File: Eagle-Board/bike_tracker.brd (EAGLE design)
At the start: 70 x 33 mm, 93 parts, among them IC1 24C00TS, IC2 BME280/680, J1 TRANSFLASH-LOCK, Q1 IRLML5203, Q2 IRLML5203, Q3 IRLML5203, Q4 IRLML5203, U1 MPU-9250/5

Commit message: minor modifications
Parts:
- moved D1 0.15 mm to (43.4, 61.9)

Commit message: last minute modifications added
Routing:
- net VBAT+: track 28.9 -> 25.1 mm

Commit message: wireless charging option added
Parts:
- added C29, C30: 22nF, resistor:C0603
- added C31, C32: 0.47uF, resistor:C0603
- added C33, C34: 0.01uF, resistor:C0603
- added C35: 100pF, resistor:C0603
- added C36: 1800pF, resistor:C0603
- added C37: 47nF, resistor:C0603
- added C38, C39: 68nF, resistor:C0603
- added C40, C41: 10uF, sparkfun:1206
- added C42, C44, C45: 0.1uF, resistor:C0603
- added C43: 1.0uF, resistor:C0603
- added COIL: 332-02, con-garry:332-02
- added D2: MBR0520, microduino:SOD123
- added R48: 196, resistor:R0603
- added R49: 75, resistor:R0603
- added R50, R52, R53: 1.5k, resistor:R0603
- added R51: 20k, resistor:R0603
- added R54: 10k NTC, resistor:R0603
- added U$3: BQ51013BQFN-20, WirelessPower:R-PVQFN-N20
- added WIR.CH.: (no value), led:SML0805
- U1: value MPU-9250/5 -> IMU9250
- moved BAT-IN 11.9 mm to (25.9, 54.8)
- moved BAT 8.60 mm to (25.9, 52.7), turned to 270 degrees
- moved LOW-BAT 1.91 mm to (6.88, 66.1)
- moved R7 0.86 mm to (9.88, 60.5)
- moved R12 0.56 mm to (27.4, 56.4)
- moved C3 0.51 mm to (23.7, 56.4)
- moved R11 0.47 mm to (29.7, 55.6)
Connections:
- new net AC1: C29.2, C31.1, C33.1, C35.1, C36.1, C37.2, C38.2, C39.2, U$3.2
- new net AC1'1: C37.1, C38.1, C39.1, COIL.1
- new net AC2: C30.1, C32.1, C34.1, C35.2, C36.2, COIL.2, U$3.19
- new net BOOT1: C33.2, U$3.3
- new net BOOT2: C34.2, U$3.17
- new net CHG: U$3.7, WIR.CH..C
- new net CLMP1: C31.2, U$3.5
- new net CLMP2: C32.2, U$3.16
- new net COMM1: C29.1, U$3.6
- new net COMM2: C30.2, U$3.15
- new net FOD: C45.1, R48.2, R49.1, R51.1, U$3.14
- new net ILIM: R49.2, U$3.12
- new net N$30: R50.1, WIR.CH..A
- new net N$31: R52.1, R54.2
- new net N$32: R53.1, R54.1
- new net OUT: C43.1, C44.1, D2.A, U$3.4
- new net RECT: C40.1, C41.1, C42.1, R50.2, R51.2, U$3.18
- new net TS-CTRL: R52.2, R53.2, U$3.13
- net 5V: now also D2.C
- net GND: now also C40.2, C41.2, C42.2, C43.2, C44.2, C45.2, R48.1, U$3.1, U$3.10, U$3.11, U$3.20, U$3.9
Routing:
- net N$30: track 0.00 -> 20.9 mm, vias 0 -> 3
- net AC2: track 0.00 -> 18.4 mm, vias 0 -> 1
- net OUT: track 0.00 -> 16.9 mm, vias 0 -> 2
- net RECT: track 0.00 -> 15.2 mm
- net AC1: track 0.00 -> 14.7 mm
- net AC1'1: track 0.00 -> 14.4 mm, vias 0 -> 1
- net GND: track 26.6 -> 40.9 mm
- net VBAT+: track 25.1 -> 39.0 mm, vias 1 -> 3
- net TS-CTRL: track 0.00 -> 13.3 mm, vias 0 -> 2
- net BOOT2: track 0.00 -> 9.91 mm, vias 0 -> 2
- net COMM2: track 0.00 -> 9.88 mm, vias 0 -> 2
- net VBAT-: track 18.0 -> 8.16 mm
- net FOD: track 0.00 -> 9.46 mm
- net CLMP2: track 0.00 -> 5.65 mm
- net COMM1: track 0.00 -> 5.29 mm
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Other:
- board size 70 x 33 mm -> 71.1 x 33 mm

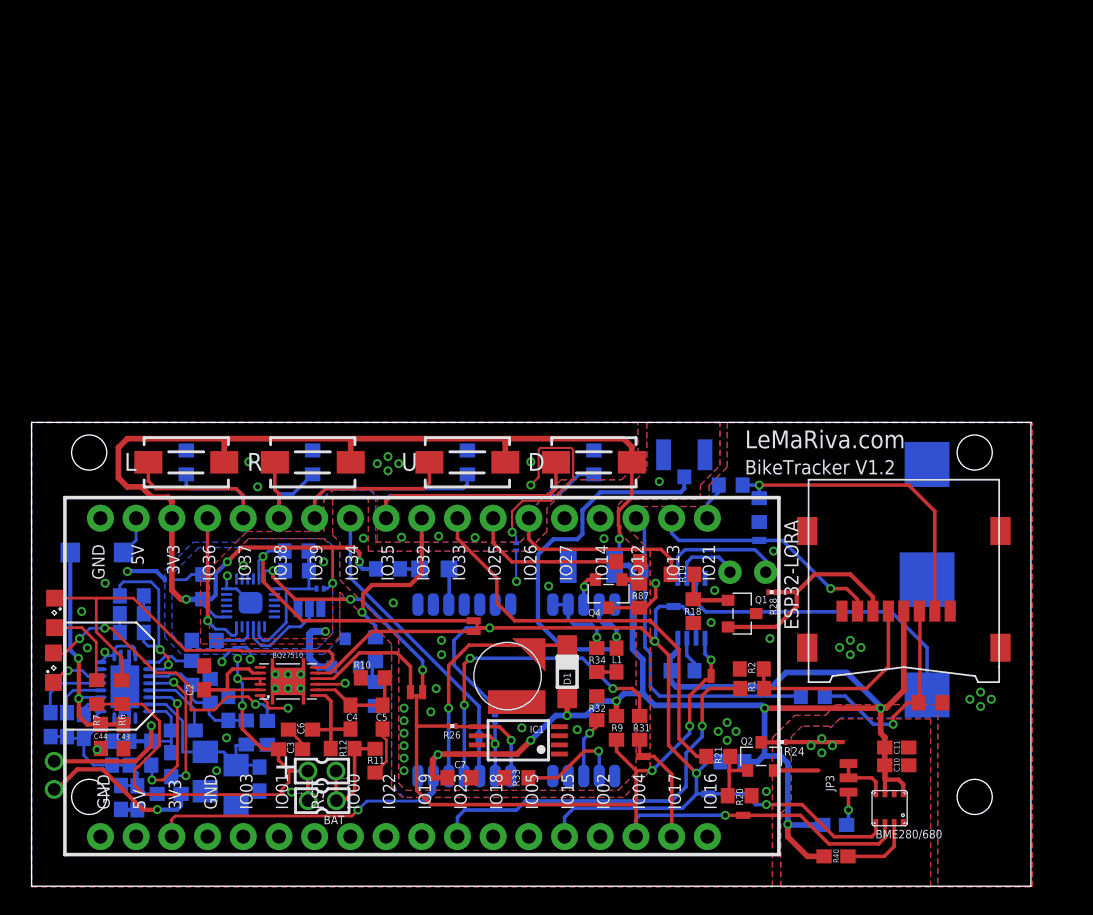
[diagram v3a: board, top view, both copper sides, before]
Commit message: added compatibility with TTGO LoRa v2.0
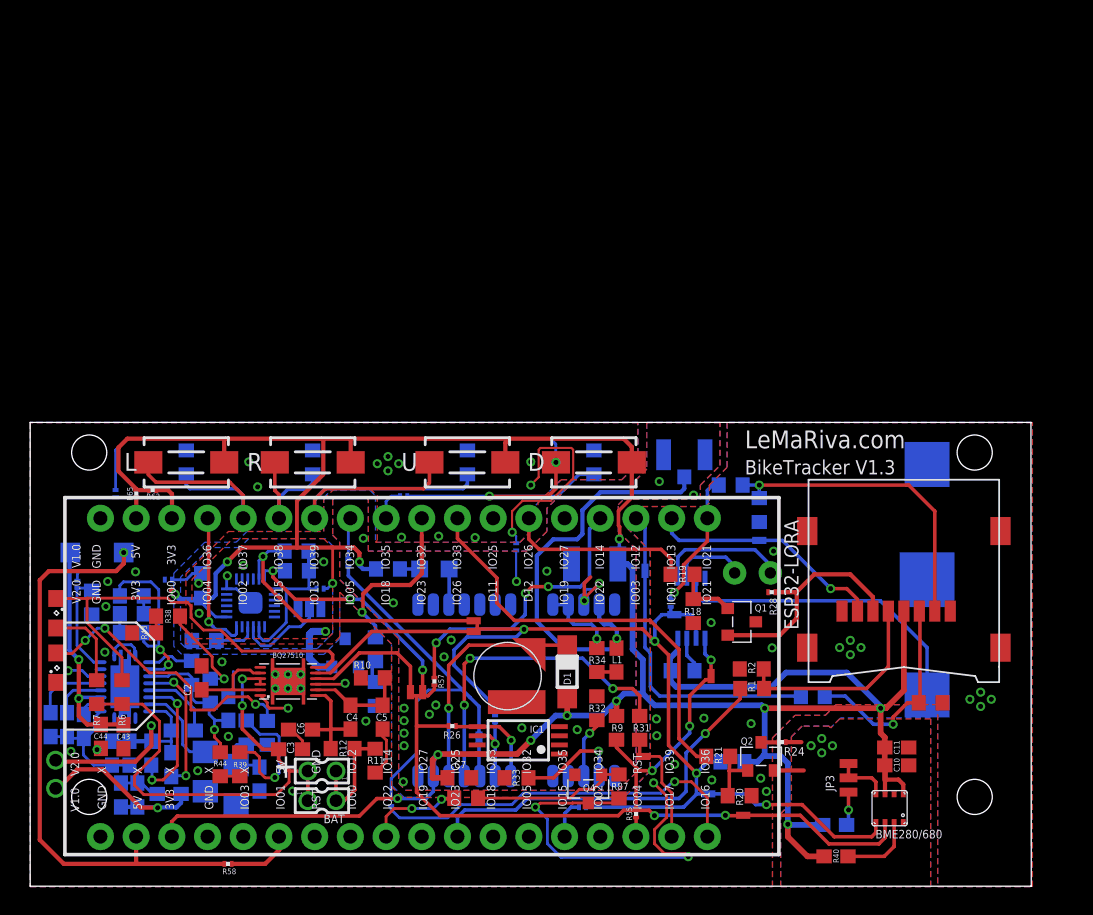
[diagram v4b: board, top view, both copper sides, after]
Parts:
- added R38, R39, R43, R44: 0, resistor:R0603
- added R45: 1M, resistor:R0603
- added R46, R47, R55, R56, R57, R58, R59, R60, R62, R63, R64, R65: (no value), resistor:R0201
- moved R90 20.4 mm to (36.2, 52.9)
- moved Q4 14.0 mm to (44.9, 53.6)
- moved R87 13.6 mm to (47.0, 53.7)
- moved SH12 0.59 mm to (50.9, 66.0)
- moved Q1 0.58 mm to (55.8, 65.5)
- moved Q5 0.33 mm to (56.5, 68.9)
- moved C1 0.25 mm to (45.3, 69.6)
- moved WIR.CH. 0.23 mm to (7.04, 62.2)
- moved C38 0.20 mm to (12.8, 53.1)
- moved C2 0.18 mm to (17.3, 61.5)
- moved C39 0.18 mm to (11.6, 53.1)
- moved LOW-BAT 0.15 mm to (7.04, 66.1)
- moved COIL 0.13 mm to (6.96, 54.6)
- moved C9 0.11 mm to (17.3, 68.0)
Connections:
- removed net 5V: D2.C, ESP32-LORA.2, ESP32-LORA.35
- removed net IO25: ESP32-LORA.25, R90.2
- new net 5V+: D2.C, ESP32-LORA.2, R46.2, R58.1
- new net GND/X: ESP32-LORA.4
- new net IO22: ESP32-LORA.9, R90.2
- new net N$28: R38.2, R48.1
- new net N$29: R39.2, R51.1
- new net N$36: R38.1, R43.2
- new net N$37: R39.1, R44.2
- new net N$38: ESP32-LORA.14, R47.1
- new net N$39: ESP32-LORA.16, R55.1
- new net N$40: ESP32-LORA.22, R57.1
- new net N$41: ESP32-LORA.29, R59.1
- new net N$42: ESP32-LORA.18, R60.2
- new net N$43: ESP32-LORA.34, R62.1
- new net N$45: ESP32-LORA.35, R63.1, R65.1
- new net N$46: ESP32-LORA.28, R64.1
- net FOD: now also R44.1; no longer R51.1
- net GND: now also R43.1, R45.2, R53.1, R54.1; no longer ESP32-LORA.4, R48.1, U$3.9
- net IO35: now also R63.2, R64.2; no longer ESP32-LORA.28
- net N$12: now also ESP32-LORA.6, R58.2; no longer ESP32-LORA.13
- net N$32: now also R45.1, R46.1, U$3.9; no longer R53.1, R54.1
- net RX: now also R59.2, R60.1; no longer ESP32-LORA.29
- net SCL: now also R47.2, R56.2; no longer ESP32-LORA.14
- net SDA: now also R55.2, R57.2; no longer ESP32-LORA.16
- net SPI-CS: now also R56.1
- net VDD: now also R62.2, R65.2; no longer ESP32-LORA.34
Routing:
- net 5V+: track 0.00 -> 46.4 mm, vias 0 -> 1
- net N$42: track 0.00 -> 27.3 mm, vias 0 -> 1
- net IO35: track 32.4 -> 57.8 mm, vias 0 -> 2
- net N$40: track 0.00 -> 20.8 mm, vias 0 -> 3
- net GND: track 40.9 -> 60.4 mm, vias 43 -> 47
- net IO25: track 11.1 -> 0.00 mm
- net N$29: track 0.00 -> 9.71 mm, vias 0 -> 1
- net RX: track 19.2 -> 27.9 mm
- net N$4: track 3.03 -> 11.0 mm
- net SPI-CS: track 2.69 -> 9.92 mm, vias 0 -> 1
- net IO22: track 0.00 -> 6.86 mm, vias 0 -> 2
- net N$28: track 0.00 -> 6.76 mm, vias 0 -> 1
- net N$32: track 1.92 -> 7.37 mm
- net N$12: track 0.00 -> 4.76 mm
- net N$45: track 0.00 -> 4.47 mm
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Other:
- board size 71.1 x 33 mm -> 71.2 x 33 mm
- board text added: "BikeTracker V1.3"
- board text removed: "BikeTracker V1.2"

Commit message: minor error correction and exported for production!
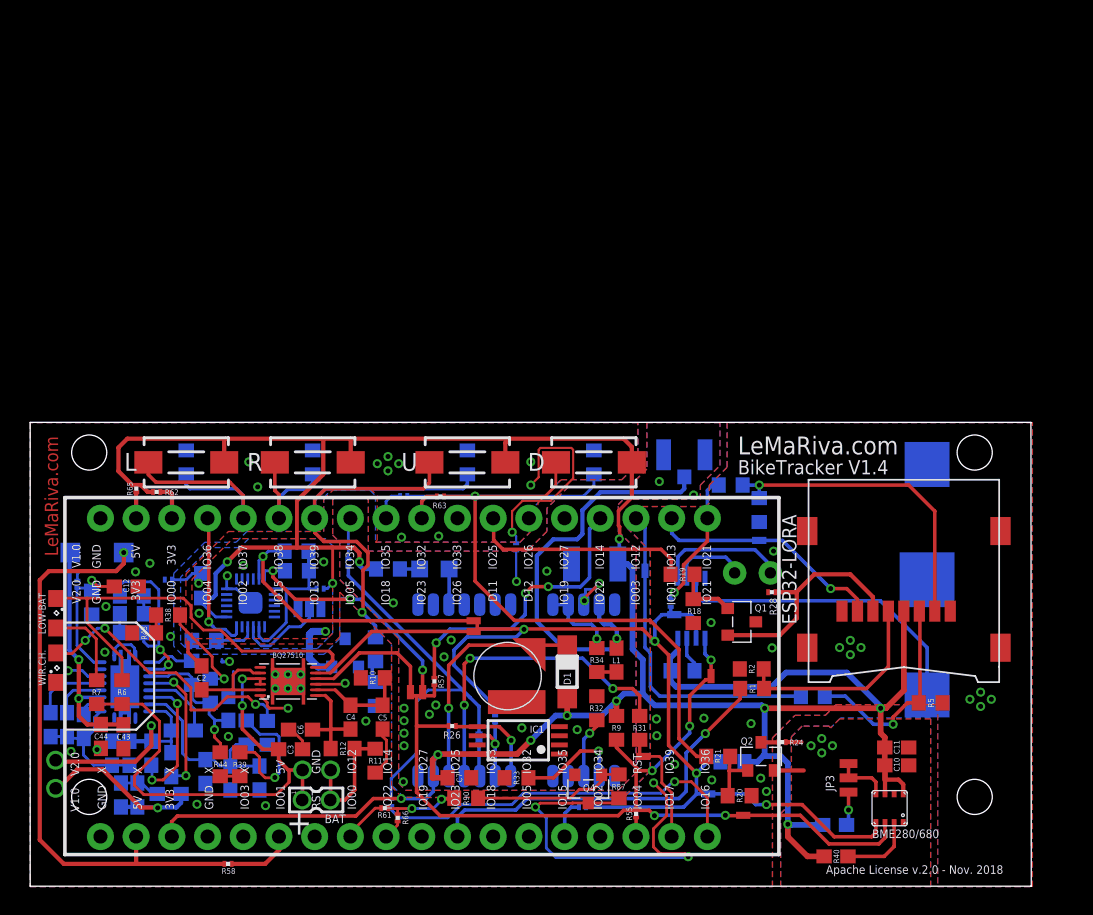
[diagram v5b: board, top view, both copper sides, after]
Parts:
- added C12: 1uF, resistor:C0603
- added R61, R66: (no value), resistor:R0201
- C40, C41: device sparkfun:1206 -> resistor:C0603
- moved R63 23.1 mm to (34.3, 74.4), flipped to the top, turned to 0 degrees
- moved C41 0.63 mm to (19.4, 54.3)
- moved BAT 0.41 mm to (25.5, 52.8)
- moved BAT-IN 0.39 mm to (25.5, 54.9), flipped to the bottom
- moved R65 0.36 mm to (12.7, 74.9)
- moved R62 0.31 mm to (14.1, 74.7)
- moved C42 0.08 mm to (21.5, 54.3)
- moved R38 0.08 mm to (15.0, 65.9)
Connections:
- removed net GND/X: ESP32-LORA.4
- removed net IO26: ESP32-LORA.24, R19.2
- removed net IO32: ESP32-LORA.27, R23.2
- removed net IO33: ESP32-LORA.26, R21.2
- new net IO25: ESP32-LORA.25, R19.2
- new net N$44: ESP32-LORA.8, R61.2
- new net N$47: ESP32-LORA.9, R66.2
- new net N$48: ESP32-LORA.27, R63.1
- net GND: now also C12.1, ESP32-LORA.4
- net IO22: now also R61.1, R66.1; no longer ESP32-LORA.9
- net IO35: now also R21.2
- net IO39: now also R23.2
- net N$32: now also C12.2
- net N$45: no longer R63.1
- net VBAT+: now also BAT-IN.1; no longer BAT-IN.2
- net VBAT-: now also BAT-IN.2; no longer BAT-IN.1
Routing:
- net IO33: track 30.3 -> 0.00 mm
- net IO25: track 0.00 -> 15.9 mm
- net IO26: track 13.3 -> 0.00 mm
- net IO32: track 12.2 -> 0.00 mm, vias 1 -> 0
- net IO39: track 24.8 -> 36.8 mm, vias 0 -> 1
- net N$44: track 0.00 -> 3.18 mm
- net GND: track 60.4 -> 63.1 mm
- net N$45: track 4.47 -> 1.85 mm
- net N$32: track 7.37 -> 9.89 mm, vias 0 -> 1
- net N$48: track 0.00 -> 2.42 mm
- net IO35: track 57.8 -> 55.7 mm, vias 2 -> 1
- net VDD: track 214.9 -> 212.9 mm, vias 13 -> 12
- net GND_GPS: track 8.00 -> 6.25 mm, vias 19 -> 18
- net N$47: track 0.00 -> 1.42 mm
- net IO22: track 6.86 -> 5.46 mm
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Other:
- board text added: "Apache License v.2.0 - Nov. 2018"
- board text added: "BikeTracker V1.4"
- board text added: "GPS-ANT"
- board text removed: "BikeTracker V1.3"
